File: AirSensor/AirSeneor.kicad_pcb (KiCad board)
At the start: 2 copper layers, 45 x 30 mm, 43 parts, among them J1 EXT_ADC, J2 SWD, J3 UART, J4 M04x2, U1 SPX3819M5, U2 MS5611, U3 LMV324, U4 MS4525DO, U5 TJA1050, U6 STM32F072CBTx, Y1 8MHz

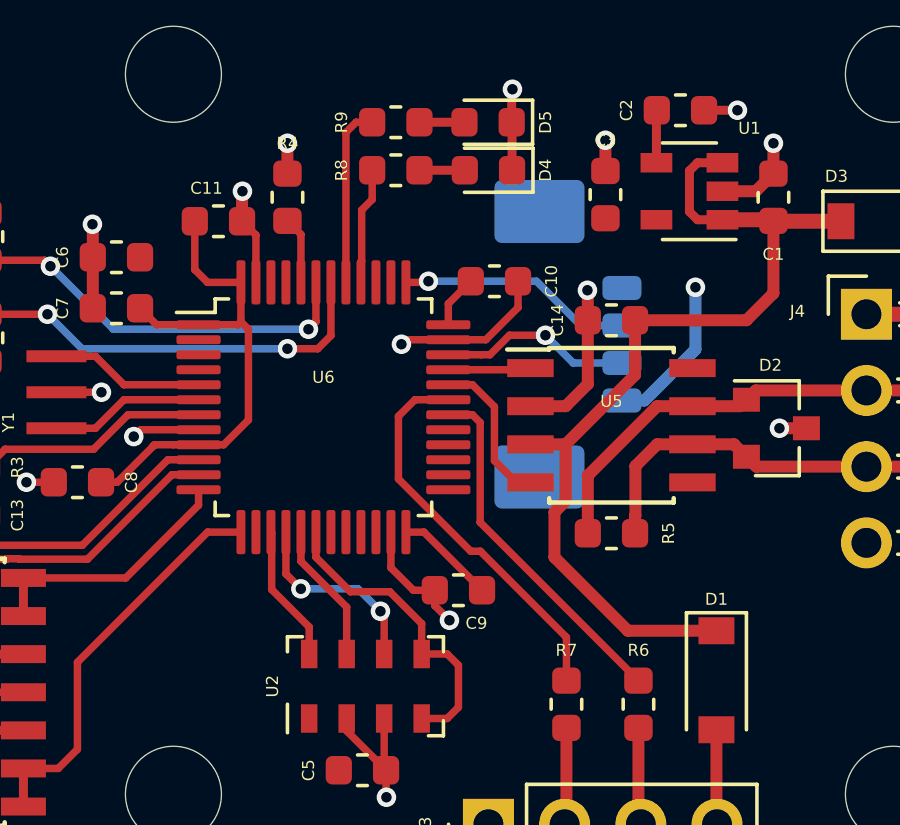
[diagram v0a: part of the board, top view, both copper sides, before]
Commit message: 1. Replace SWD connector with 10 pin SMD 2x5 connector in AirSensor. 2. Add signal name silk screen in AirSensor.
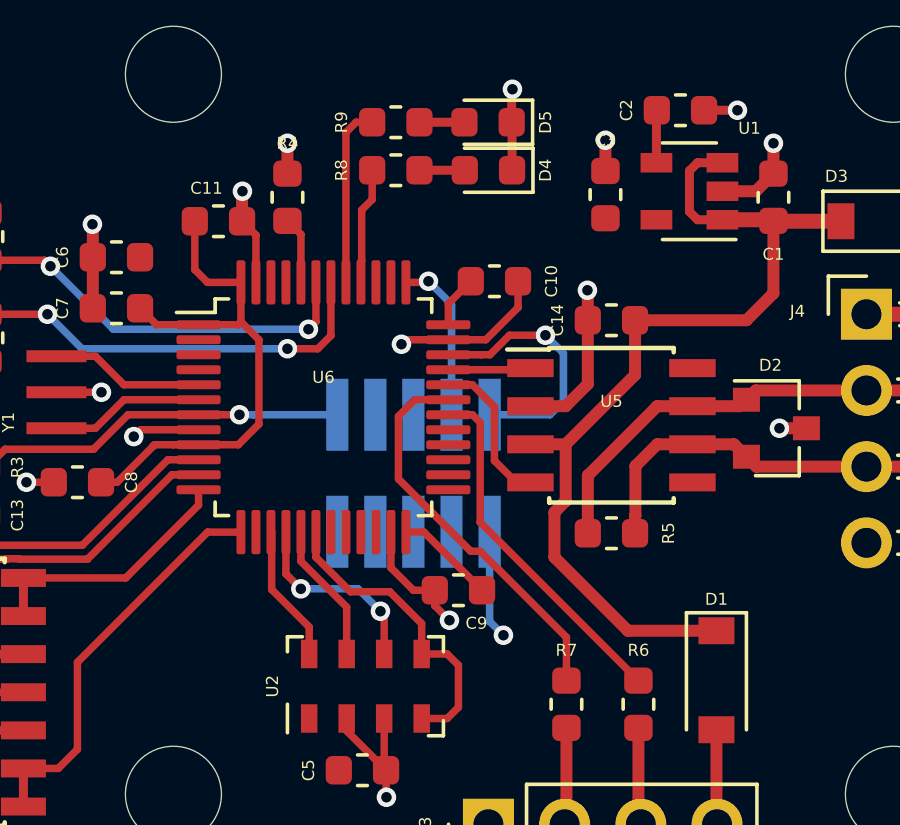
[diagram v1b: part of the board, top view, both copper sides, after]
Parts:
- J2: value SWD -> Conn_SWD; footprint Connector_Molex:Molex_PicoBlade_53398-0471_1x04-1MP_P1.25mm_Vertical -> Connector_PinHeader_1.27mm:PinHeader_2x05_P1.27mm_Vertical_SMD
- U1: value SPX3819M5 -> SPX3819M5-L-3-3
- moved J2 7.14 mm to (143.0, 114.3)
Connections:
- C13 pad 1: Net-(C13-Pad1) -> nRST
- J1 pad 2: A3 -> A0
- J1 pad 4: A0 -> A2
- J1 pad 5: A2 -> A3
- J2 pad 3: SWCLK -> GND
- J2 pad 4: GND -> SWCLK
- R3 pad 1: Net-(C13-Pad1) -> nRST
- U3 pad 10: A3 -> A0
- U3 pad 12: A2 -> A3
- U3 pad 3: A0 -> A2
- U6 pad 7: Net-(C13-Pad1) -> nRST
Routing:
- net nRST: track 0.00 -> 14.0 mm, vias 0 -> 1
- net Net-(C13-Pad1): track 9.37 -> 0.00 mm
- net A2: track 12.0 -> 5.74 mm
- net A0: track 5.74 -> 11.5 mm
- net SWCLK: track 7.83 -> 5.53 mm
- net SWDIO: track 6.44 -> 8.60 mm
- net +3V3: track 33.9 -> 32.9 mm
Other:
- board text added: "3V3"
- board text added: "5V"
- board text added: "A0"
- board text added: "A1"
- board text added: "A2"
- board text added: "A3"
- board text added: "CANH"
- board text added: "CANL"
- board text added: "GND"
- board text added: "RX"
- board text added: "SWD"
- board text added: "TX"

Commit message: Update schematics and PCB print for AirSensor.
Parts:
- U1: value SPX3819M5-L-3-3 -> SPX3819M5
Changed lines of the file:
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@@
       (effects (font (size 0.4 0.4) (thickness 0.1)))
     )
-    (fp_text value SPX3819M5-L-3-3 (at 0 -2.2 180) (layer F.Fab)
+    (fp_text value SPX3819M5 (at 0 -2.2 180) (layer F.Fab)
       (effects (font (size 0.4 0.4) (thickness 0.1)))
     )
@@
   (segment (start 137.162002 113.35) (end 137.850001 112.662001) (width 0.25) (layer F.Cu) (net 4))
   (segment (start 135.8375 113.35) (end 137.162002 113.35) (width 0.25) (layer F.Cu) (net 4))
-  (segment (start 133.48641 112.35) (end 132.33641 113.5) (width 0.25) (layer F.Cu) (net 61))
-  (segment (start 135.8375 112.35) (end 133.48641 112.35) (width 0.25) (layer F.Cu) (net 61))
-  (segment (start 129.3875 113.5) (end 128.7875 114.1) (width 0.25) (layer F.Cu) (net 61))
-  (segment (start 132.33641 113.5) (end 129.3875 113.5) (width 0.25) (layer F.Cu) (net 61))
-  (segment (start 128.7875 115.7) (end 128.7875 114.1) (width 0.25) (layer F.Cu) (net 61))
   (segment (start 153.1 125.98) (end 153.12 126) (width 0.4) (layer F.Cu) (net 5))
   (segment (start 153.1 122.85) (end 153.1 125.98) (width 0.4) (layer F.Cu) (net 5))
@@
   (segment (start 132.4 112.8) (end 131.1 112.8) (width 0.25) (layer F.Cu) (net 42))
   (segment (start 133.35 111.85) (end 132.4 112.8) (width 0.25) (layer F.Cu) (net 42))
-  (via (at 128.3 123) (size 0.65) (drill 0.35) (layers F.Cu B.Cu) (net 60))
-  (segment (start 130 122.87) (end 128.43 122.87) (width 0.3) (layer F.Cu) (net 60))
-  (segment (start 128.43 122.87) (end 128.3 123) (width 0.3) (layer F.Cu) (net 60))
-  (segment (start 127.3 124) (end 119 124) (width 0.3) (layer B.Cu) (net 60))
-  (segment (start 128.3 123) (end 127.3 124) (width 0.3) (layer B.Cu) (net 60))
   (via (at 128.2 119.6) (size 0.65) (drill 0.35) (layers F.Cu B.Cu) (net 57))
   (segment (start 130 120.33) (end 128.93 120.33) (width 0.3) (layer F.Cu) (net 57))
@@
   (segment (start 126.6 118) (end 119 118) (width 0.3) (layer B.Cu) (net 57))
   (segment (start 128.2 119.6) (end 126.6 118) (width 0.3) (layer B.Cu) (net 57))
+  (via (at 122.8 120.2) (size 0.65) (drill 0.35) (layers F.Cu B.Cu) (net 58))
+  (segment (start 122.93 120.33) (end 122.8 120.2) (width 0.3) (layer F.Cu) (net 58))
+  (segment (start 124.6 120.33) (end 122.93 120.33) (width 0.3) (layer F.Cu) (net 58))
+  (segment (start 122.6 120) (end 122.8 120.2) (width 0.3) (layer B.Cu) (net 58))
+  (segment (start 119 120) (end 122.6 120) (width 0.3) (layer B.Cu) (net 58))
   (via (at 121.2 122.4) (size 0.65) (drill 0.35) (layers F.Cu B.Cu) (net 59))
   (segment (start 123.6 122.87) (end 124.6 122.87) (width 0.25) (layer F.Cu) (net 59))
@@
   (segment (start 120.8 122) (end 121.2 122.4) (width 0.25) (layer B.Cu) (net 59))
   (segment (start 119 122) (end 120.8 122) (width 0.25) (layer B.Cu) (net 59))
-  (via (at 122.8 120.2) (size 0.65) (drill 0.35) (layers F.Cu B.Cu) (net 58))
-  (segment (start 122.93 120.33) (end 122.8 120.2) (width 0.3) (layer F.Cu) (net 58))
-  (segment (start 124.6 120.33) (end 122.93 120.33) (width 0.3) (layer F.Cu) (net 58))
-  (segment (start 122.6 120) (end 122.8 120.2) (width 0.3) (layer B.Cu) (net 58))
-  (segment (start 119 120) (end 122.6 120) (width 0.3) (layer B.Cu) (net 58))
+  (via (at 128.3 123) (size 0.65) (drill 0.35) (layers F.Cu B.Cu) (net 60))
+  (segment (start 130 122.87) (end 128.43 122.87) (width 0.3) (layer F.Cu) (net 60))
+  (segment (start 128.43 122.87) (end 128.3 123) (width 0.3) (layer F.Cu) (net 60))
+  (segment (start 127.3 124) (end 119 124) (width 0.3) (layer B.Cu) (net 60))
+  (segment (start 128.3 123) (end 127.3 124) (width 0.3) (layer B.Cu) (net 60))
+  (segment (start 133.48641 112.35) (end 132.33641 113.5) (width 0.25) (layer F.Cu) (net 61))
+  (segment (start 135.8375 112.35) (end 133.48641 112.35) (width 0.25) (layer F.Cu) (net 61))
+  (segment (start 129.3875 113.5) (end 128.7875 114.1) (width 0.25) (layer F.Cu) (net 61))
+  (segment (start 132.33641 113.5) (end 129.3875 113.5) (width 0.25) (layer F.Cu) (net 61))
+  (segment (start 128.7875 115.7) (end 128.7875 114.1) (width 0.25) (layer F.Cu) (net 61))
   (via (at 137.2 112.35) (size 0.65) (drill 0.35) (layers F.Cu B.Cu) (net 61))
   (segment (start 135.8375 112.35) (end 137.2 112.35) (width 0.25) (layer F.Cu) (net 61))
